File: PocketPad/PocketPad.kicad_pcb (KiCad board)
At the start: 2 copper layers, 75 x 65 mm, 43 parts, among them SW0 SW_Push, SW1 SW_Push, SW10 SW_Push, SW11 SW_Push, SW12 SW_Push, SW13 SW_Push, SW14 SW_Push, SW15 SW_Push, SW16 SW_Push, SW17 SW_Push, SW2 SW_Push, SW3 SW_Push, SW4 SW_Push, SW5 SW_Push, SW6 SW_Push, SW7 SW_Push, SW8 SW_Push, SW9 SW_Push

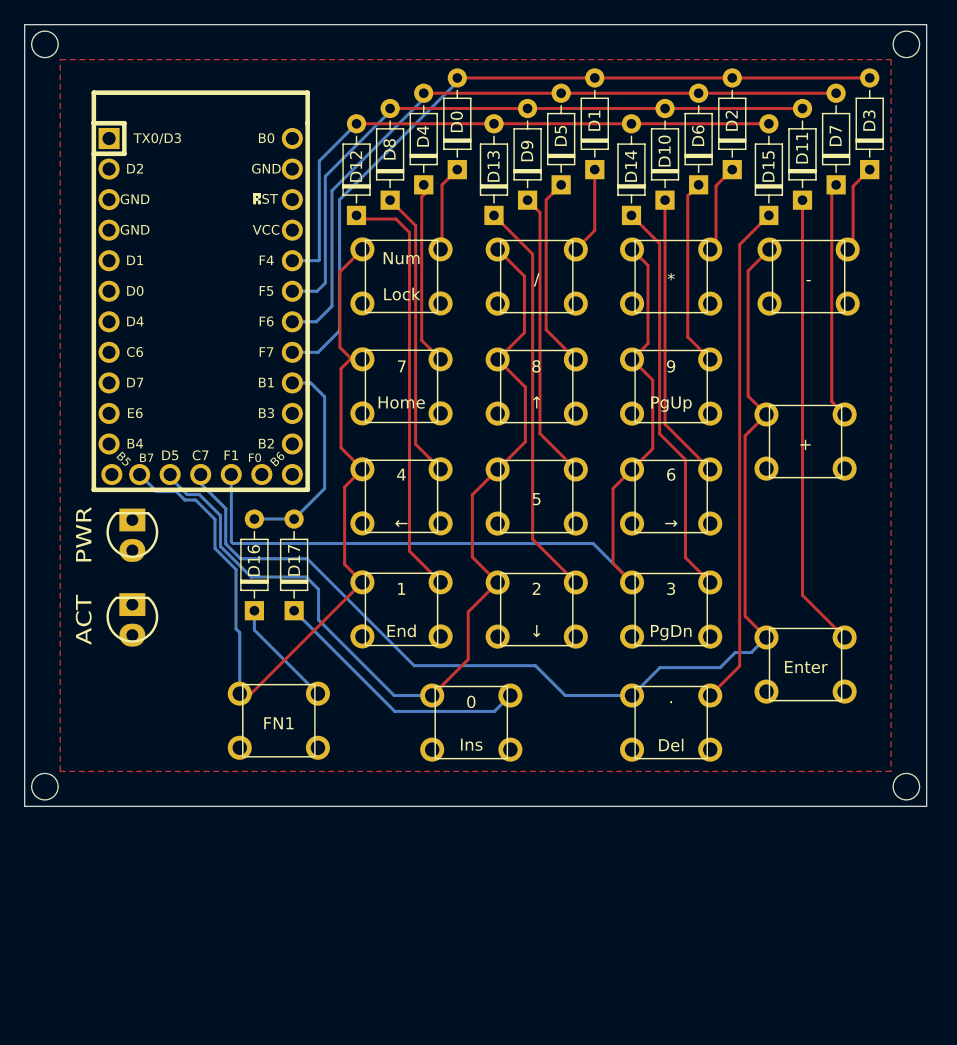
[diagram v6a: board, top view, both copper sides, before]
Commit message: symbols updated. PCB redone.
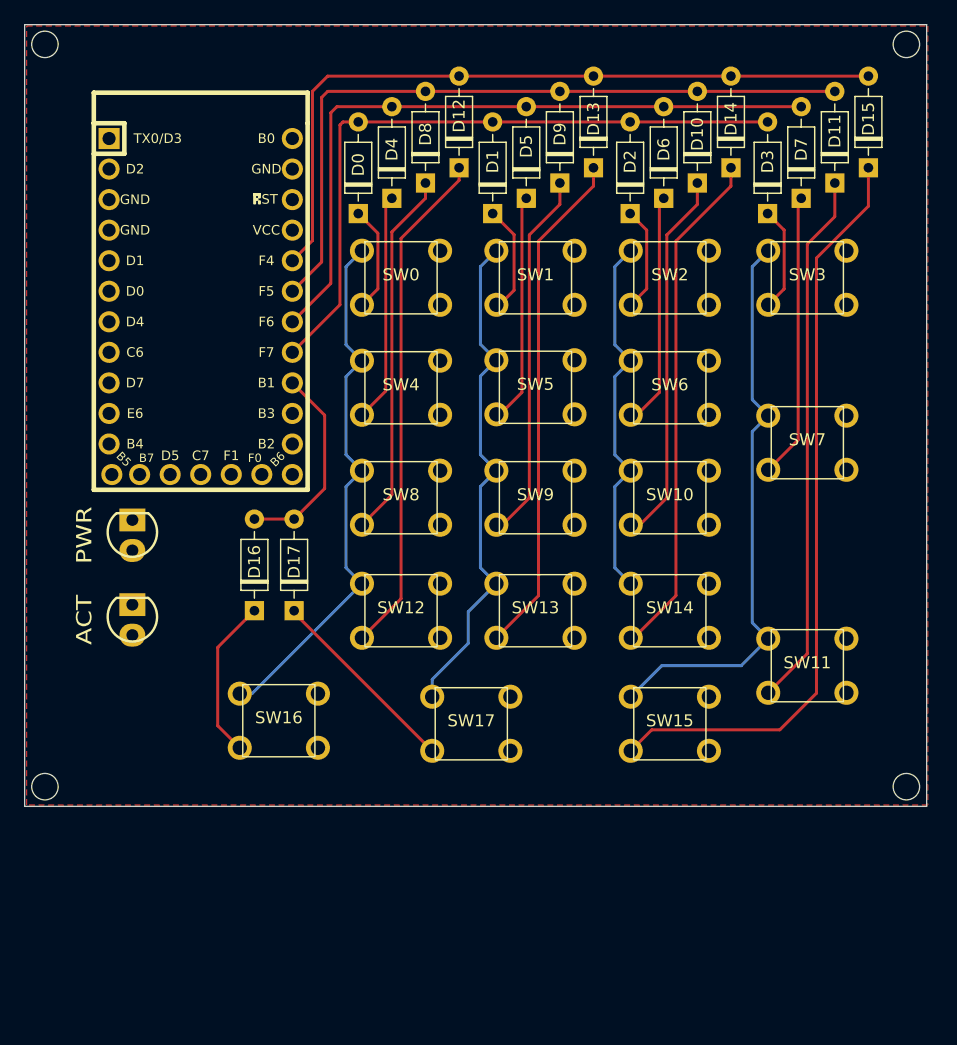
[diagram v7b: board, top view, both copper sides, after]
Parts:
- SW0, SW1, SW10, SW11, SW12, SW13, SW14, SW15, SW16, SW17, SW2, SW3, SW4, SW5, SW6, SW7, SW8, SW9: value SW_Push -> SW_THT_6x6
- moved D12 9.40 mm to (58.2, 28.4)
- moved D3 9.24 mm to (83.8, 32.3)
- moved D1 9.24 mm to (61.0, 32.3)
- moved D2 9.24 mm to (72.4, 32.3)
- moved D13 9.17 mm to (69.3, 28.4)
- moved D14 9.17 mm to (80.8, 28.4)
- moved D15 9.17 mm to (92.2, 28.4)
- moved D0 9.01 mm to (49.8, 32.3)
- moved D8 3.27 mm to (55.4, 29.7)
- moved D5 3.11 mm to (63.8, 31.0)
- moved D6 3.11 mm to (75.2, 31.0)
- moved D7 3.11 mm to (86.6, 31.0)
- moved D11 3.04 mm to (89.4, 29.7)
- moved D9 3.04 mm to (66.5, 29.7)
- moved D10 3.04 mm to (78.0, 29.7)
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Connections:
- D0 pad 1: Net-(D0-Pad1) -> Net-(SW0-Pad3)
- D1 pad 1: Net-(D1-Pad1) -> Net-(SW1-Pad3)
- D10 pad 1: Net-(D10-Pad1) -> Net-(SW10-Pad3)
- D11 pad 1: Net-(D11-Pad1) -> Net-(SW11-Pad3)
- D12 pad 1: Net-(D12-Pad1) -> Net-(SW12-Pad3)
- D13 pad 1: Net-(D13-Pad1) -> Net-(SW13-Pad3)
- D14 pad 1: Net-(D14-Pad1) -> Net-(SW14-Pad3)
- D15 pad 1: Net-(D15-Pad1) -> Net-(SW15-Pad3)
- D16 pad 1: Net-(D16-Pad1) -> Net-(SW16-Pad3)
- D17 pad 1: Net-(D17-Pad1) -> Net-(SW17-Pad3)
- D2 pad 1: Net-(D2-Pad1) -> Net-(SW2-Pad3)
- D3 pad 1: Net-(D3-Pad1) -> Net-(SW3-Pad3)
- D4 pad 1: Net-(D4-Pad1) -> Net-(SW4-Pad3)
- D5 pad 1: Net-(D5-Pad1) -> Net-(SW5-Pad3)
- D7 pad 1: Net-(D7-Pad1) -> Net-(SW7-Pad3)
- D8 pad 1: Net-(D8-Pad1) -> Net-(SW8-Pad3)
- D9 pad 1: Net-(D9-Pad1) -> Net-(SW9-Pad3)
- SW0 pad 2: Net-(D0-Pad1) -> unconnected-(SW0-Pad2)
- SW0 pad 3: (no net) -> Net-(SW0-Pad3)
- SW0 pad 4: (no net) -> unconnected-(SW0-Pad4)
- SW1 pad 2: Net-(D1-Pad1) -> unconnected-(SW1-Pad2)
- SW1 pad 3: (no net) -> Net-(SW1-Pad3)
- SW1 pad 4: (no net) -> unconnected-(SW1-Pad4)
- SW10 pad 2: Net-(D10-Pad1) -> unconnected-(SW10-Pad2)
- SW10 pad 3: (no net) -> Net-(SW10-Pad3)
- SW10 pad 4: (no net) -> unconnected-(SW10-Pad4)
- SW11 pad 2: Net-(D11-Pad1) -> unconnected-(SW11-Pad2)
- SW11 pad 3: (no net) -> Net-(SW11-Pad3)
- SW11 pad 4: (no net) -> unconnected-(SW11-Pad4)
- SW12 pad 2: Net-(D12-Pad1) -> unconnected-(SW12-Pad2)
- SW12 pad 3: (no net) -> Net-(SW12-Pad3)
- SW12 pad 4: (no net) -> unconnected-(SW12-Pad4)
- SW13 pad 2: Net-(D13-Pad1) -> unconnected-(SW13-Pad2)
- SW13 pad 3: (no net) -> Net-(SW13-Pad3)
- SW13 pad 4: (no net) -> unconnected-(SW13-Pad4)
- SW14 pad 2: Net-(D14-Pad1) -> unconnected-(SW14-Pad2)
- SW14 pad 3: (no net) -> Net-(SW14-Pad3)
- SW14 pad 4: (no net) -> unconnected-(SW14-Pad4)
- SW15 pad 2: Net-(D15-Pad1) -> unconnected-(SW15-Pad2)
- SW15 pad 3: (no net) -> Net-(SW15-Pad3)
- SW15 pad 4: (no net) -> unconnected-(SW15-Pad4)
- SW16 pad 2: Net-(D16-Pad1) -> unconnected-(SW16-Pad2)
- SW16 pad 3: (no net) -> Net-(SW16-Pad3)
- SW16 pad 4: (no net) -> unconnected-(SW16-Pad4)
- SW17 pad 2: Net-(D17-Pad1) -> unconnected-(SW17-Pad2)
- SW17 pad 3: (no net) -> Net-(SW17-Pad3)
- SW17 pad 4: (no net) -> unconnected-(SW17-Pad4)
- SW2 pad 2: Net-(D2-Pad1) -> unconnected-(SW2-Pad2)
- SW2 pad 3: (no net) -> Net-(SW2-Pad3)
- SW2 pad 4: (no net) -> unconnected-(SW2-Pad4)
- SW3 pad 2: Net-(D3-Pad1) -> unconnected-(SW3-Pad2)
- SW3 pad 3: (no net) -> Net-(SW3-Pad3)
- SW3 pad 4: (no net) -> unconnected-(SW3-Pad4)
- SW4 pad 2: Net-(D4-Pad1) -> unconnected-(SW4-Pad2)
- SW4 pad 3: (no net) -> Net-(SW4-Pad3)
- SW4 pad 4: (no net) -> unconnected-(SW4-Pad4)
- SW5 pad 2: Net-(D5-Pad1) -> unconnected-(SW5-Pad2)
- SW5 pad 3: (no net) -> Net-(SW5-Pad3)
- SW5 pad 4: (no net) -> unconnected-(SW5-Pad4)
- SW6 pad 2: Net-(D6-Pad1) -> unconnected-(SW6-Pad2)
- SW6 pad 3: (no net) -> Net-(D6-Pad1)
- SW6 pad 4: (no net) -> unconnected-(SW6-Pad4)
- SW7 pad 2: Net-(D7-Pad1) -> unconnected-(SW7-Pad2)
- SW7 pad 3: (no net) -> Net-(SW7-Pad3)
- SW7 pad 4: (no net) -> unconnected-(SW7-Pad4)
- SW8 pad 2: Net-(D8-Pad1) -> unconnected-(SW8-Pad2)
- SW8 pad 3: (no net) -> Net-(SW8-Pad3)
- SW8 pad 4: (no net) -> unconnected-(SW8-Pad4)
- SW9 pad 2: Net-(D9-Pad1) -> unconnected-(SW9-Pad2)
- SW9 pad 3: (no net) -> Net-(SW9-Pad3)
- SW9 pad 4: (no net) -> unconnected-(SW9-Pad4)
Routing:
- net Net-(SW15-Pad3): track 0.00 -> 62.9 mm
- net COL3: track 93.9 -> 47.9 mm
- net Net-(SW11-Pad3): track 0.00 -> 44.7 mm
- net Net-(SW14-Pad3): track 0.00 -> 42.4 mm
- net Net-(SW13-Pad3): track 0.00 -> 42.4 mm
- net Net-(SW12-Pad3): track 0.00 -> 42.4 mm
- net Net-(D15-Pad1): track 41.9 -> 0.00 mm
- net COL2: track 71.8 -> 31.0 mm
- net Net-(D11-Pad1): track 37.8 -> 0.00 mm
- net Net-(D12-Pad1): track 35.2 -> 0.00 mm
- net COL1: track 77.4 -> 42.6 mm
- net Net-(D13-Pad1): track 33.3 -> 0.00 mm
- net Net-(D14-Pad1): track 33.2 -> 0.00 mm
- net Net-(SW8-Pad3): track 0.00 -> 30.6 mm
- net Net-(SW9-Pad3): track 0.00 -> 30.4 mm
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
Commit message: V1 complete
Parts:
- added ACT-R1: 1k, Resistor_THT:R_Axial_DIN0207_L6.3mm_D2.5mm_P10.16mm_Horizontal, F.Cu at (35.6, 75.4)
- added PWR-R1: 1k, Resistor_THT:R_Axial_DIN0207_L6.3mm_D2.5mm_P10.16mm_Horizontal, F.Cu at (25.4, 72.1)
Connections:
- ACT pad 1: unconnected-(ACTLED1-Pad1) -> Net-(ACT-R1-Pad1)
- ACT pad 2: unconnected-(ACTLED1-Pad2) -> Net-(ACT1-Pad2)
- MCU1 pad 11: unconnected-(MCU1-Pad11) -> Net-(ACT1-Pad2)
- MCU1 pad 12: unconnected-(MCU1-Pad12) -> Net-(PWR1-Pad2)
- MCU1 pad 25: COL0 -> COL3
- MCU1 pad 26: COL1 -> COL2
- MCU1 pad 27: COL3 -> COL1
- MCU1 pad 28: COL2 -> COL0
- PWR pad 1: unconnected-(PWRLED1-Pad1) -> Net-(PWR-R1-Pad2)
- PWR pad 2: unconnected-(PWRLED1-Pad2) -> Net-(PWR1-Pad2)
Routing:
- net COL3: track 47.9 -> 120.2 mm
- net COL2: track 31.0 -> 99.8 mm
- net COL1: track 42.6 -> 81.8 mm
- net COL0: track 44.9 -> 63.5 mm
- net Net-(ACT1-Pad2): track 0.00 -> 16.3 mm
- net Net-(PWR-R1-Pad2): track 0.00 -> 13.8 mm
- net Net-(ACT-R1-Pad1): track 0.00 -> 10.0 mm
- net Net-(PWR1-Pad2): track 0.00 -> 4.48 mm
